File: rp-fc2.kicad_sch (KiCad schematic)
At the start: 32 parts, among them CN1 20021521-00010T1LF, SW1 SW_Push, U1 RP2350A-QFN60, U2 W25Q128JVS, Y1 Crystal_GND24

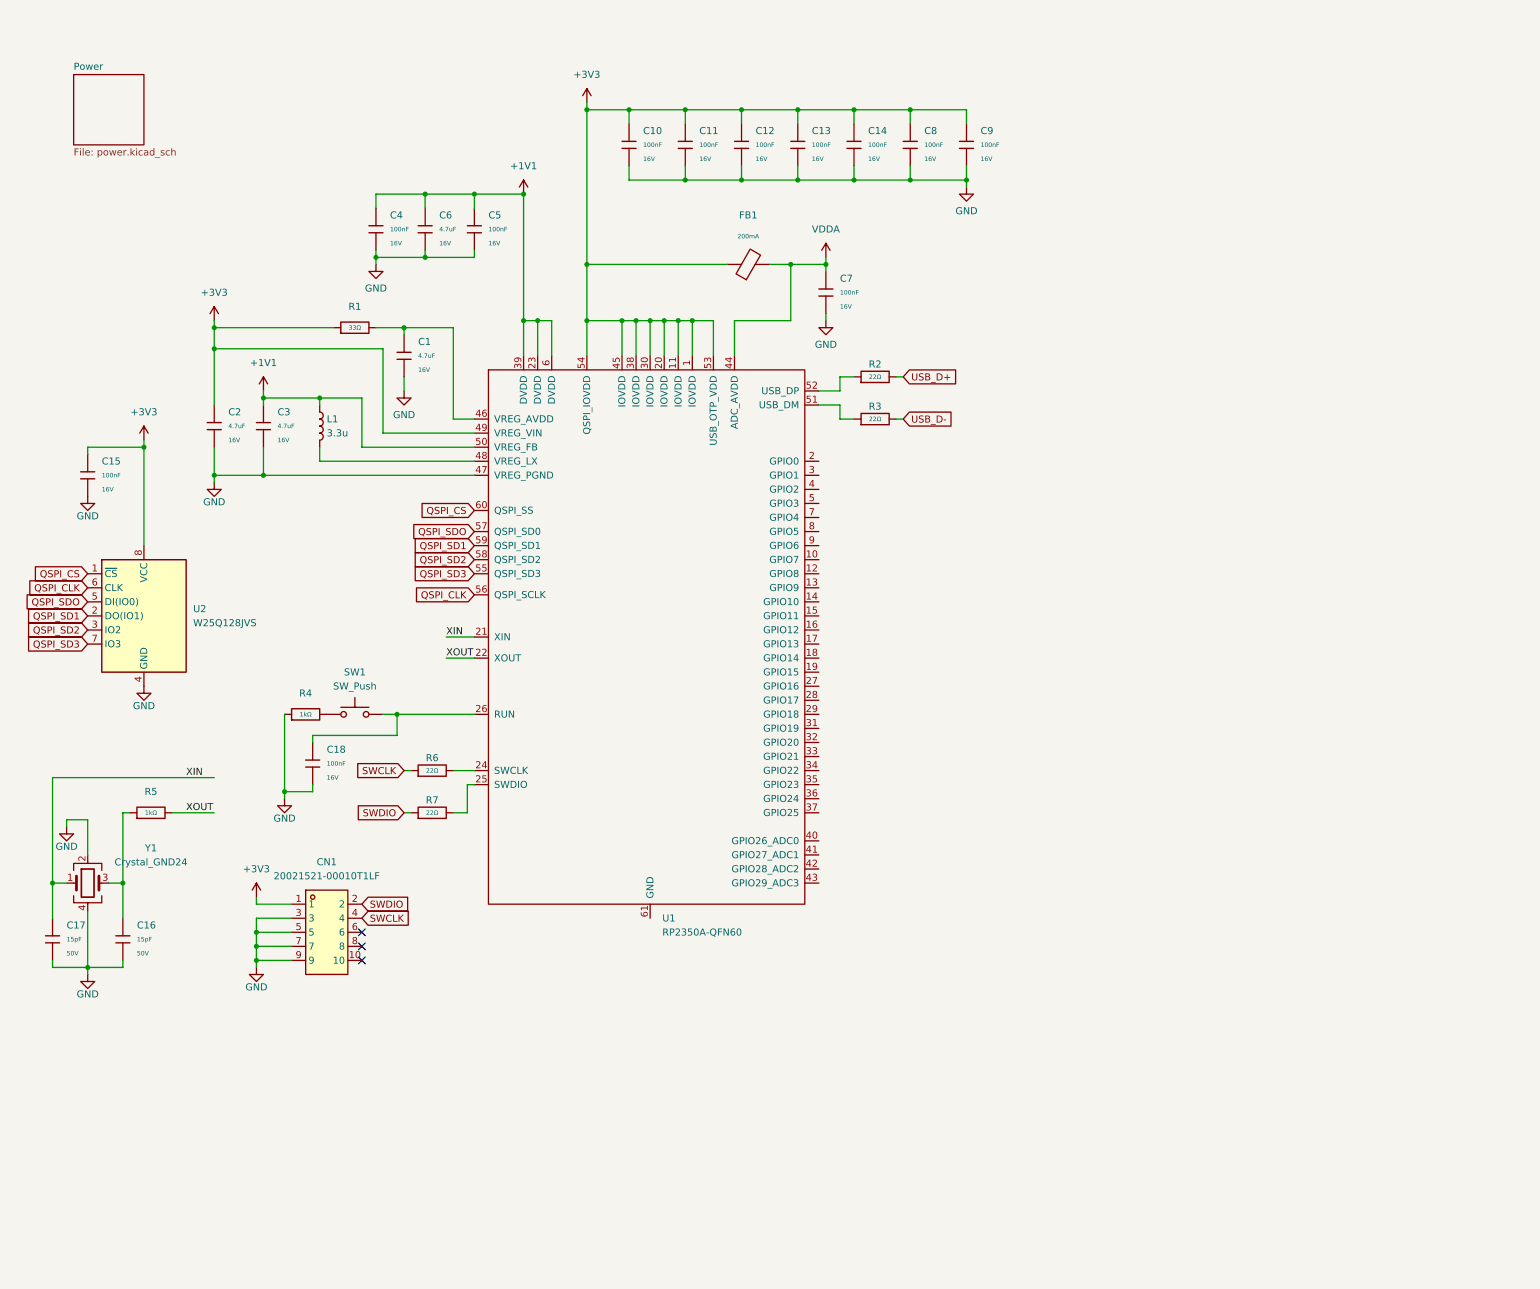
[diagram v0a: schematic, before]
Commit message: rp2350 power + servo rails
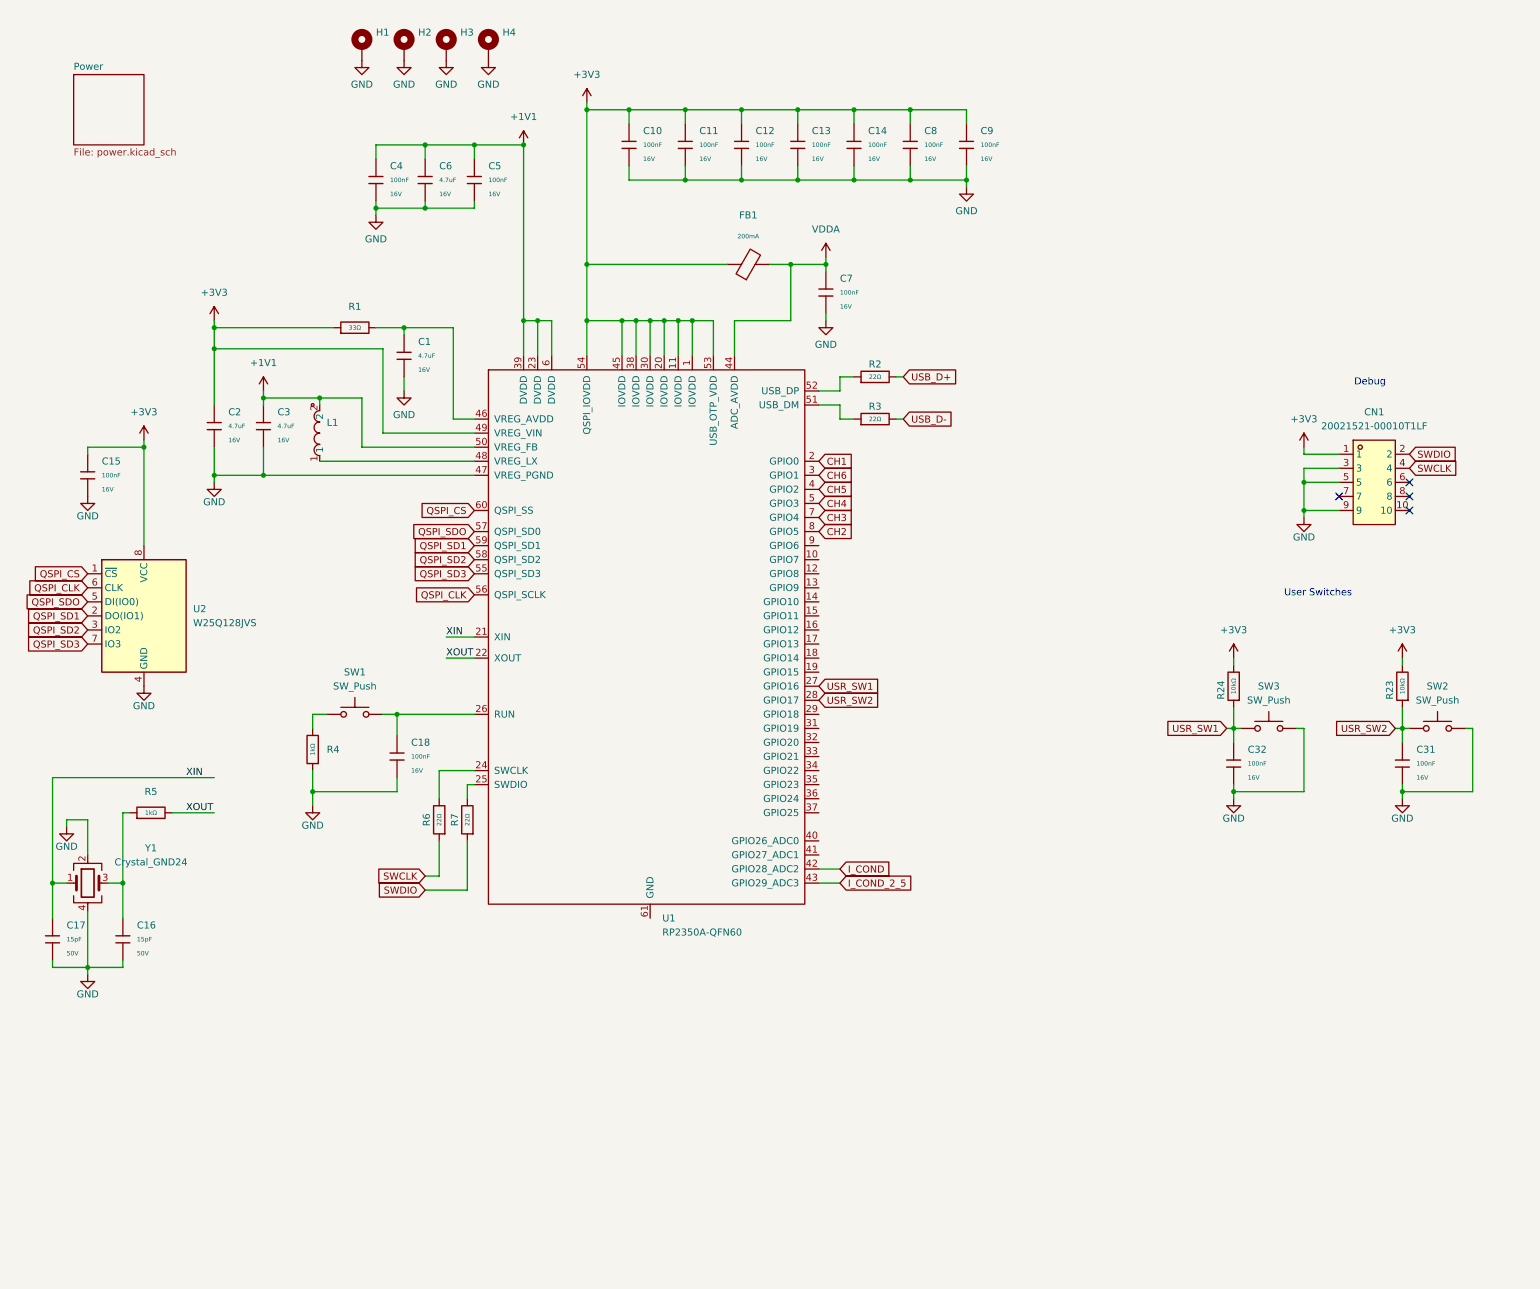
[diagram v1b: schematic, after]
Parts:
- removed L1: 3.3u, Inductor_SMD:L_Murata_DFE201610P, symbol Device:L
- added C31, C32: 100nF, PCM_JLCPCB:C_0402, symbol JLCPCB-Capacitors:0402,100nF
- added H1, H2, H3, H4: MountingHole_Pad, MountingHole:MountingHole_2.2mm_M2_DIN965_Pad, symbol Mechanical:MountingHole_Pad
- added L1: AOTA-B201610S3R3-101-T, easyeda2kicad:IND-SMD_L2.0-W1.6_AOTA-B201610S3R3-101-T, symbol easyeda2kicad:AOTA-B201610S3R3-101-T
- added R23, R24: 10kΩ, PCM_JLCPCB:R_0402, symbol JLCPCB-Resistors:0402,10kΩ
- added SW2, SW3: SW_Push, Button_Switch_THT:SW_PUSH_1P1T_6x3.5mm_H4.3_APEM_MJTP1243, symbol Switch:SW_Push
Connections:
- net +1V1: now also L1.2
- net +3V3: now also R23.2, R24.2
- net GND: now also C31.2, C32.2, H1.1, H2.1, H3.1, H4.1, SW2.2, SW3.2; no longer CN1.7
- net CH1: now reaches U1.2 (GPIO0)
- net USR_SW1: now reaches U1.27 (GPIO16)
- net USR_SW1: now also C32.1, R24.1, SW3.1
- net USR_SW2: now reaches U1.28 (GPIO17)
- net USR_SW2: now also C31.1, R23.1, SW2.1
- net CH6: now reaches U1.3 (GPIO1)
- net CH5: now reaches U1.4 (GPIO2)
- net I_COND: now reaches U1.42 (GPIO28_ADC2)
- net I_COND_2_5: now reaches U1.43 (GPIO29_ADC3)
- net at U1.48 (VREG_LX): now also L1.1
- net CH4: now reaches U1.5 (GPIO3)
- net CH3: now reaches U1.7 (GPIO4)
- net CH2: now reaches U1.8 (GPIO5)
- no-connect marks 3 -> 4
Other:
- note added: "Debug"
- note added: "User Switches"
- moved on the sheet: C18, C4, C5, C6, CN1, R7

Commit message: add camera breakout
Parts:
- removed C31: 100nF, PCM_JLCPCB:C_0402, symbol JLCPCB-Capacitors:0402,100nF
- removed R23: 10kΩ, PCM_JLCPCB:R_0402, symbol JLCPCB-Resistors:0402,10kΩ
- removed SW2: SW_Push, Button_Switch_THT:SW_PUSH_1P1T_6x3.5mm_H4.3_APEM_MJTP1243, symbol Switch:SW_Push
- added R23, R25, R26, R27, R28, R29, R30, R31, R32: 22Ω, PCM_JLCPCB:R_0402, symbol JLCPCB-Resistors:0402,22Ω
- added R33, R34: 4.7kΩ, PCM_JLCPCB:R_0402, symbol JLCPCB-Resistors:0402,4.7kΩ
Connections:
- net +3V3: now also R33.1, R34.1
- net USR_SW1: now also U1.32 (GPIO20); no longer U1.27 (GPIO16)
- net at U1.10 (GPIO7): now also R25.1
- net at U1.12 (GPIO8): now also R26.1
- net at U1.13 (GPIO9): now also R27.1
- net at U1.14 (GPIO10): now also R28.1
- net at U1.15 (GPIO11): now also R29.1
- net at U1.16 (GPIO12): now also R30.1
- net at U1.17 (GPIO13): now also R31.1
- net XCLK: now reaches U1.18 (GPIO14)
- net at U1.19 (GPIO15): now also R32.1
- net SIO_D: now reaches U1.29 (GPIO18)
- net SIO_D: now also R33.2
- net SIO_C: now reaches U1.31 (GPIO19)
- net SIO_C: now also R34.2
- net at U1.9 (GPIO6): now also R23.1
- net USR_SW2 renamed VSYNC
- new net D0: R23.2
- new net D1: R25.2
- new net D2: R26.2
- new net D3: R27.2
- new net D4: R28.2
- new net D5: R29.2
- new net D6: R30.2
- new net D7: R31.2
- new net HREF: U1.27 (GPIO16)
- new net PCLK: R32.2
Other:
- added sheet Breakouts (breakouts.kicad_sch)
- note removed: "User Switches"
- moved on the sheet: C32, R24, SW3

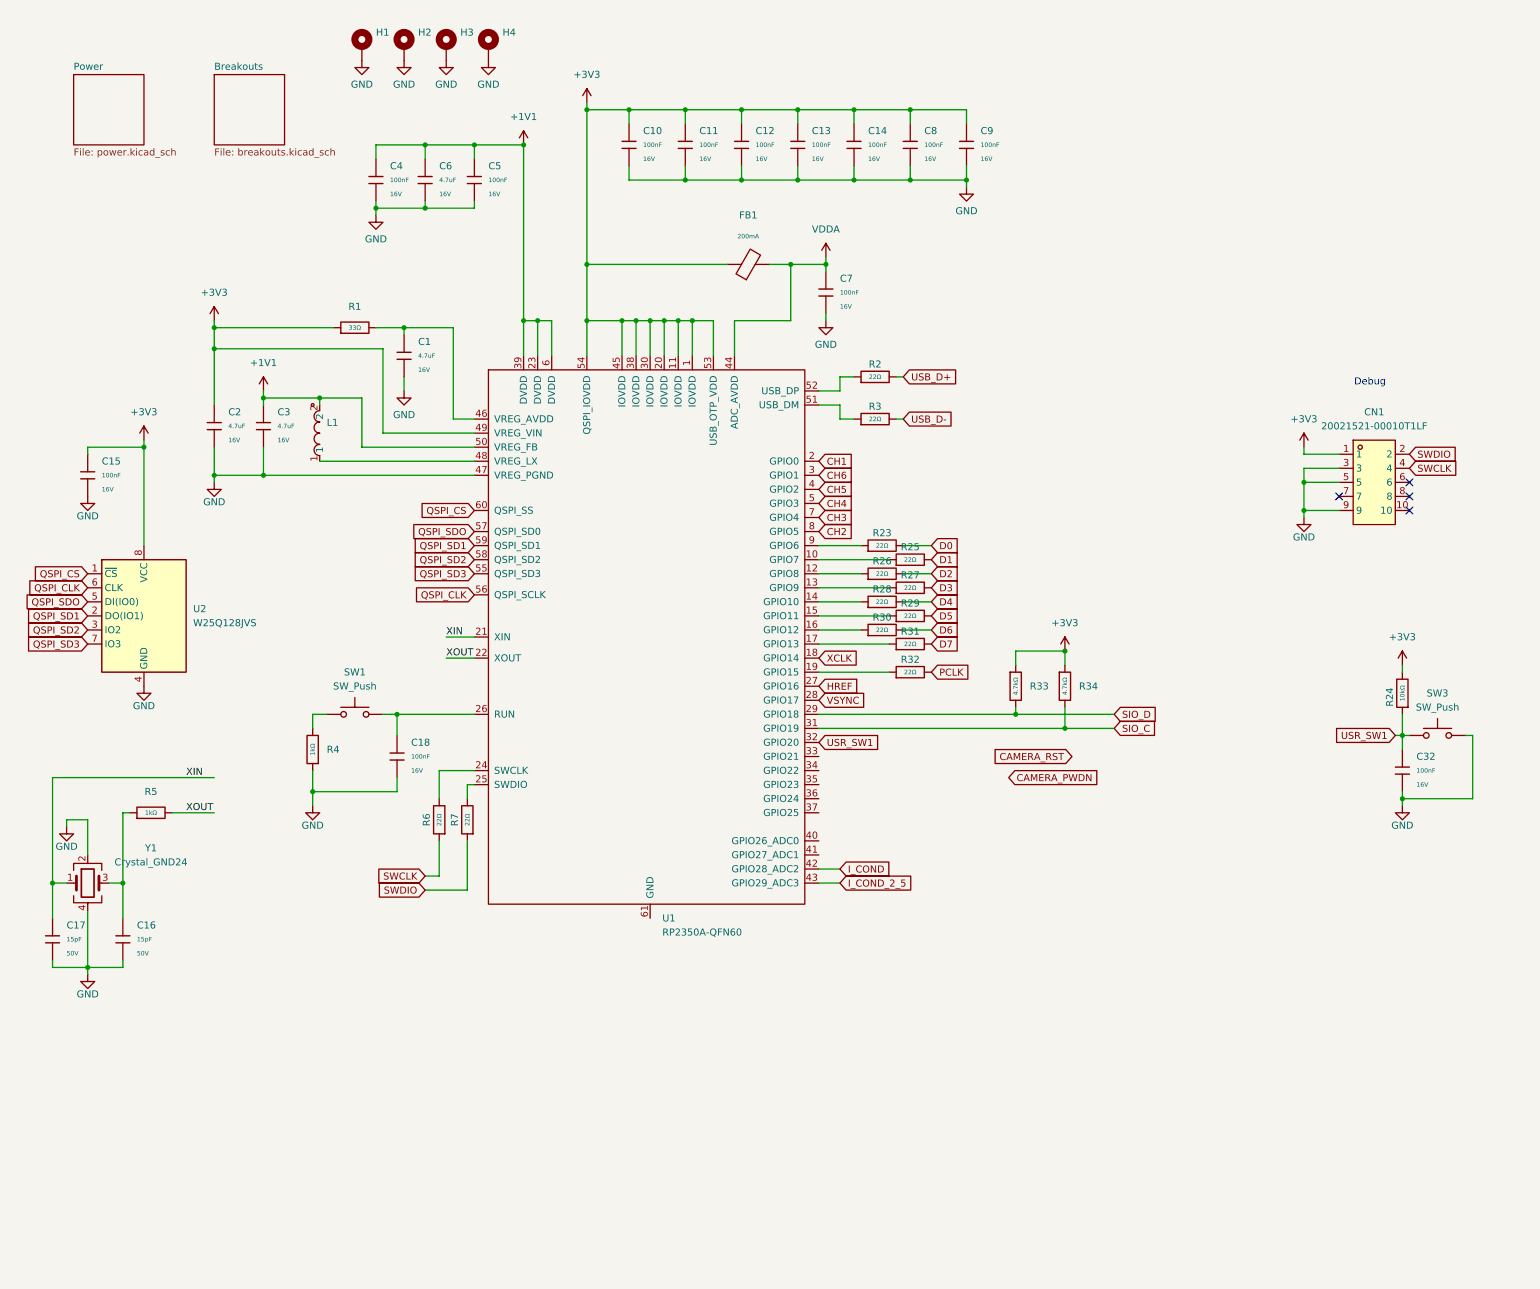
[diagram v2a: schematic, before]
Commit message: rp2350B -- larger package
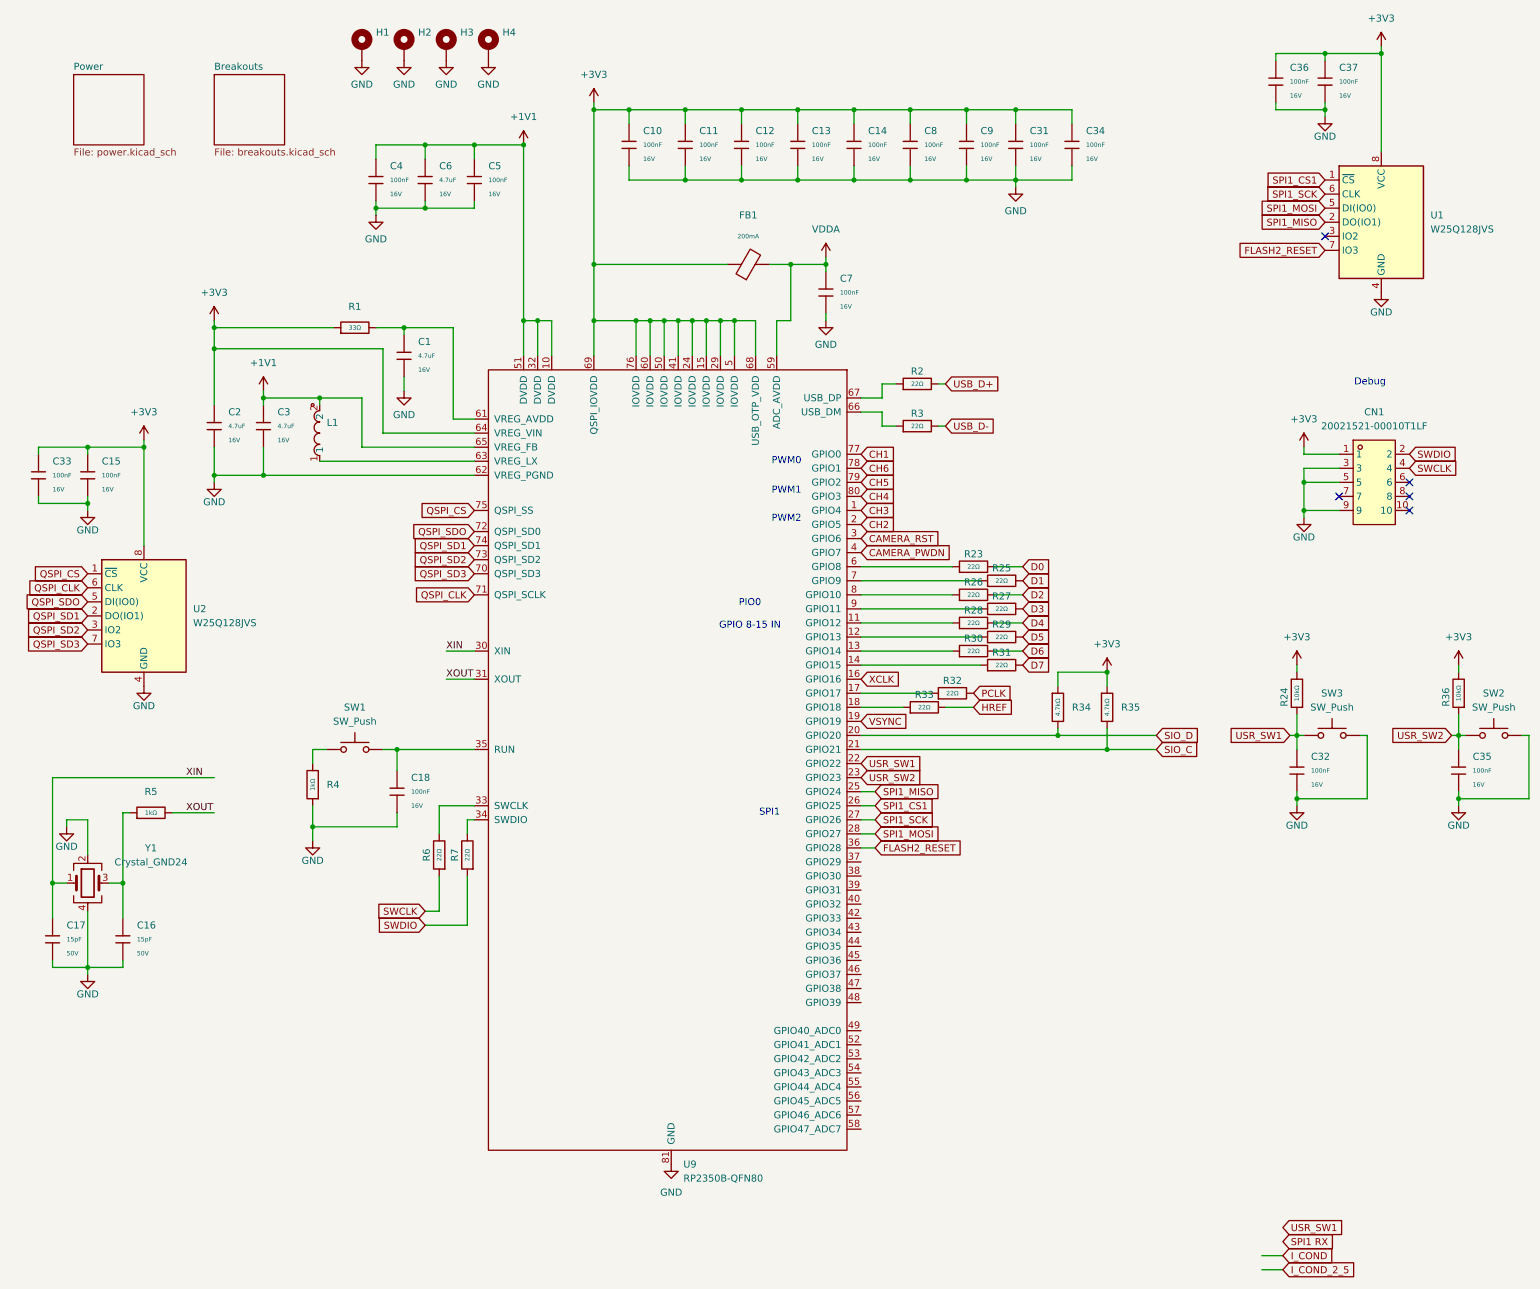
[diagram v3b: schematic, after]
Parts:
- removed R33: 4.7kΩ, PCM_JLCPCB:R_0402, symbol JLCPCB-Resistors:0402,4.7kΩ
- removed U1: RP2350A-QFN60, RP2350_KiCad:RP2350A_QFN-60_EP_7.75x7.75_Pitch0.4mm, symbol RP2350A:RP2350A-QFN60
- added C31, C33, C34, C35, C36, C37: 100nF, PCM_JLCPCB:C_0402, symbol JLCPCB-Capacitors:0402,100nF
- added R33: 22Ω, PCM_JLCPCB:R_0402, symbol JLCPCB-Resistors:0402,22Ω
- added R35: 4.7kΩ, PCM_JLCPCB:R_0402, symbol JLCPCB-Resistors:0402,4.7kΩ
- added R36: 10kΩ, PCM_JLCPCB:R_0402, symbol JLCPCB-Resistors:0402,10kΩ
- added SW2: SW_Push, Button_Switch_THT:SW_PUSH_1P1T_6x3.5mm_H4.3_APEM_MJTP1243, symbol Switch:SW_Push
- added U1: W25Q128JVS, Package_SO:SOIC-8_5.23x5.23mm_P1.27mm, symbol Memory_Flash:W25Q128JVS
- added U9: RP2350B-QFN80, RP2350_KiCad:RP2350B_QFN-80_EP_10.573x10.573_Pitch0.4mm, symbol RP2350B:RP2350B-QFN80
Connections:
- net +1V1: now also U9.10 (DVDD), U9.32 (DVDD), U9.51 (DVDD), U9.65 (VREG_FB)
- net +3V3: now also C31.1, C33.1, C34.1, C36.1, C37.1, R35.1, R36.2, U1.8 (VCC), U9.15 (IOVDD), U9.24 (IOVDD), U9.29 (IOVDD), U9.41 (IOVDD), U9.5 (IOVDD), U9.50 (IOVDD), U9.60 (IOVDD), U9.64 (VREG_VIN), U9.68 (USB_OTP_VDD), U9.69 (QSPI_IOVDD), U9.76 (IOVDD)
- net CAMERA_PWDN: now also U9.4 (GPIO7)
- net CAMERA_RST: now also U9.3 (GPIO6)
- net CH1: now also U9.77 (GPIO0)
- net CH2: now also U9.2 (GPIO5)
- net CH3: now also U9.1 (GPIO4)
- net CH4: now also U9.80 (GPIO3)
- net CH5: now also U9.79 (GPIO2)
- net CH6: now also U9.78 (GPIO1)
- net GND: now also C31.2, C33.2, C34.2, C35.2, C36.2, C37.2, SW2.2, U1.4 (GND), U9.62 (VREG_PGND), U9.81 (GND)
- net HREF: now also R33.2
- net QSPI_CLK: now also U9.71 (QSPI_SCLK)
- net QSPI_CS: now also U9.75 (QSPI_SS)
- net QSPI_SD1: now also U9.74 (QSPI_SD1)
- net QSPI_SD2: now also U9.73 (QSPI_SD2)
- net QSPI_SD3: now also U9.70 (QSPI_SD3)
- net QSPI_SDO: now also U9.72 (QSPI_SD0)
- net SIO_C: now also R35.2, U9.21 (GPIO21); no longer R34.2
- net SIO_D: now also R34.2, U9.20 (GPIO20)
- net USR_SW1: now also U9.22 (GPIO22)
- net VDDA: now also U9.59 (ADC_AVDD)
- net VSYNC: now also U9.19 (GPIO19)
- net XCLK: now also U9.16 (GPIO16)
- net XIN: now also U9.30 (XIN)
- net XOUT: now also U9.31 (XOUT)
- net at C18.1, SW1.2: now also U9.35 (RUN)
- net at R31.1: now also U9.14 (GPIO15)
- net at R32.1: now also U9.17 (GPIO17)
- net at R7.2: now also U9.34 (SWDIO)
- net at R23.1: now also U9.6 (GPIO8)
- net at R6.2: now also U9.33 (SWCLK)
- net at R26.1: now also U9.8 (GPIO10)
- net at R25.1: now also U9.7 (GPIO9)
- net at R27.1: now also U9.9 (GPIO11)
- net at R28.1: now also U9.11 (GPIO12)
- net at R29.1: now also U9.12 (GPIO13)
- net at R30.1: now also U9.13 (GPIO14)
- net at C1.1, R1.2: now also U9.61 (VREG_AVDD)
- net at L1.1: now also U9.63 (VREG_LX)
- net at R3.1: now also U9.66 (USB_DM)
- net at R2.1: now also U9.67 (USB_DP)
- new net: R33.1, U9.18 (GPIO18)
- new net FLASH2_RESET: U1.7 (IO3), U9.36 (GPIO28)
- new net SPI1_CS1: U1.1 (~{CS}), U9.26 (GPIO25)
- new net SPI1_MISO: U1.2 (DO(IO1)), U9.25 (GPIO24)
- new net SPI1_MOSI: U1.5 (DI(IO0)), U9.28 (GPIO27)
- new net SPI1_SCK: U1.6 (CLK), U9.27 (GPIO26)
- new net USR_SW2: C35.1, R36.1, SW2.1, U9.23 (GPIO23)
- no-connect marks 4 -> 5
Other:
- note added: "PIO0 GPIO 8-15 IN"
- note added: "PWM0"
- note added: "PWM1"
- note added: "PWM2"
- note added: "SPI1"
- moved on the sheet: C18, C32, R24, R4, R6, R7, SW1, SW3
